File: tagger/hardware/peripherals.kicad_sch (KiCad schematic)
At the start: 15 parts, among them J2 MICRO_SD_CARD, U1 LSM6DS3, U8 MAX98357A, U9 W25Q128JVP

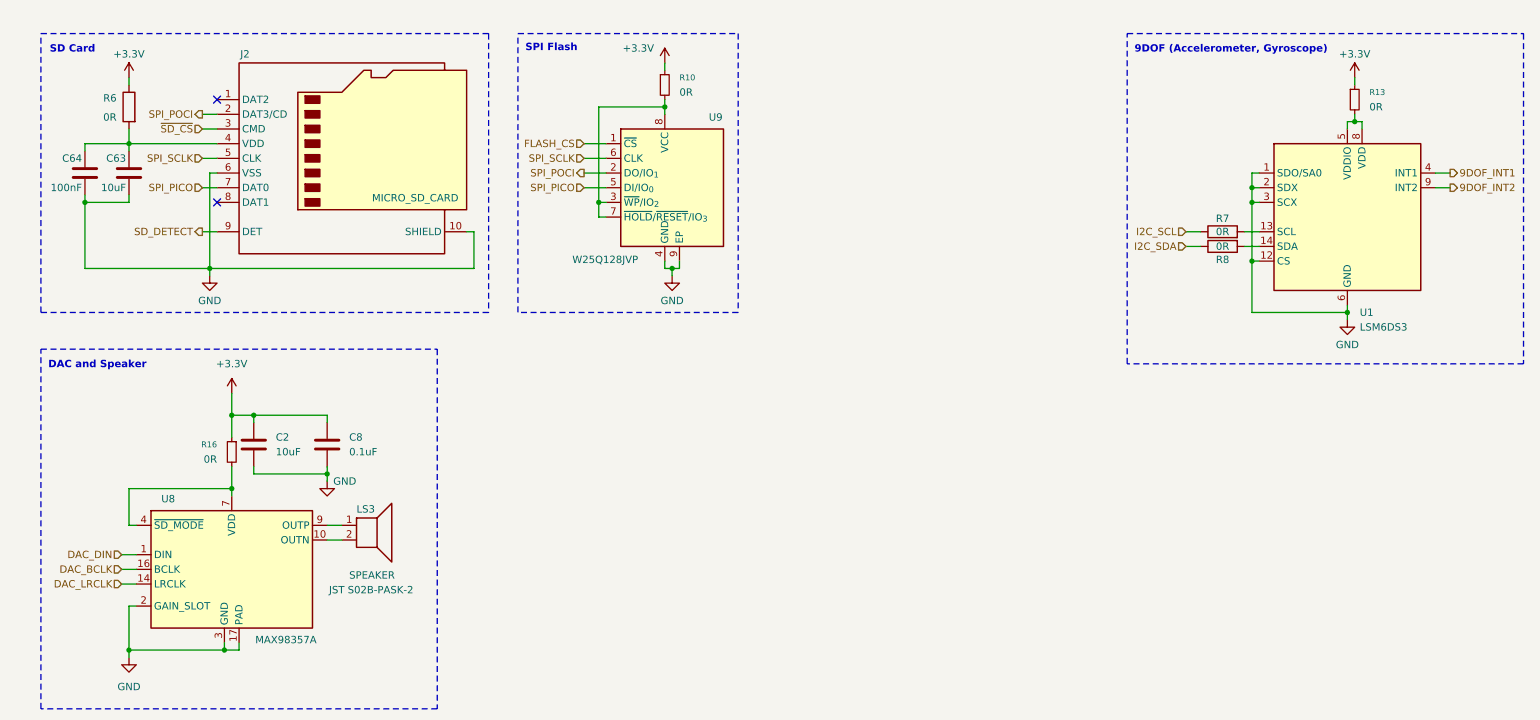
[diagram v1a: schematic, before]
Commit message: feat: various board routing changes
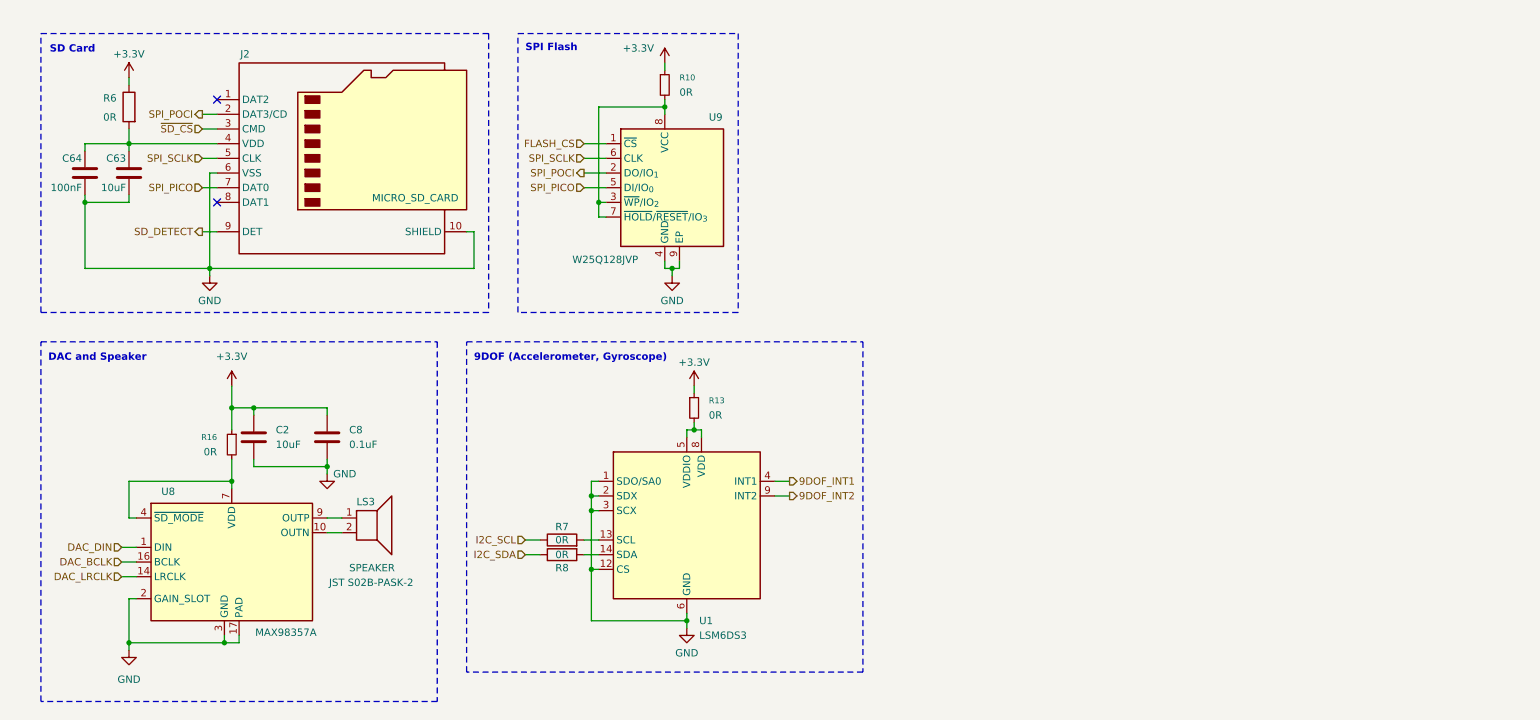
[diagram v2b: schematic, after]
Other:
- moved on the sheet: C2, C8, LS3, R13, R16, R7, R8, U1, U8

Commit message: feat: add IR routing, fix component sizes
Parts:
- C2, C63, C64, C8: footprint Capacitor_SMD:C_0201_0603Metric_Pad0.64x0.40mm_HandSolder -> Capacitor_SMD:C_0402_1005Metric
- R10, R13, R16, R6, R7, R8: footprint Resistor_SMD:R_0201_0603Metric_Pad0.64x0.40mm_HandSolder -> Resistor_SMD:R_0402_1005Metric
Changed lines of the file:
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@@
 			)
 		)
-		(property "Footprint" "Resistor_SMD:R_0201_0603Metric_Pad0.64x0.40mm_HandSolder"
+		(property "Footprint" "Resistor_SMD:R_0402_1005Metric"
 			(at 128.27 27.94 0)
 			(effects
@@
 			)
 		)
-		(property "Footprint" "Resistor_SMD:R_0201_0603Metric_Pad0.64x0.40mm_HandSolder"
+		(property "Footprint" "Resistor_SMD:R_0402_1005Metric"
 			(at 110.49 107.442 90)
 			(effects
@@
 			)
 		)
-		(property "Footprint" "Capacitor_SMD:C_0201_0603Metric_Pad0.64x0.40mm_HandSolder"
+		(property "Footprint" "Capacitor_SMD:C_0402_1005Metric"
 			(at 34.5948 46.99 0)
 			(effects
@@
 			)
 		)
-		(property "Footprint" "Capacitor_SMD:C_0201_0603Metric_Pad0.64x0.40mm_HandSolder"
+		(property "Footprint" "Capacitor_SMD:C_0402_1005Metric"
 			(at 58.1152 92.71 0)
 			(effects
@@
 			)
 		)
-		(property "Footprint" "Resistor_SMD:R_0201_0603Metric_Pad0.64x0.40mm_HandSolder"
+		(property "Footprint" "Resistor_SMD:R_0402_1005Metric"
 			(at 37.338 31.75 90)
 			(effects
@@
 			)
 		)
-		(property "Footprint" "Resistor_SMD:R_0201_0603Metric_Pad0.64x0.40mm_HandSolder"
+		(property "Footprint" "Resistor_SMD:R_0402_1005Metric"
 			(at 110.49 108.458 90)
 			(effects
@@
 			)
 		)
-		(property "Footprint" "Resistor_SMD:R_0201_0603Metric_Pad0.64x0.40mm_HandSolder"
+		(property "Footprint" "Resistor_SMD:R_0402_1005Metric"
 			(at 133.35 83.82 0)
 			(effects
@@
 			)
 		)
-		(property "Footprint" "Resistor_SMD:R_0201_0603Metric_Pad0.64x0.40mm_HandSolder"
+		(property "Footprint" "Resistor_SMD:R_0402_1005Metric"
 			(at 53.34 90.17 0)
 			(effects
@@
 			)
 		)
-		(property "Footprint" "Capacitor_SMD:C_0201_0603Metric_Pad0.64x0.40mm_HandSolder"
+		(property "Footprint" "Capacitor_SMD:C_0402_1005Metric"
 			(at 70.8152 92.71 0)
 			(effects
@@
 			)
 		)
-		(property "Footprint" "Capacitor_SMD:C_0201_0603Metric_Pad0.64x0.40mm_HandSolder"
+		(property "Footprint" "Capacitor_SMD:C_0402_1005Metric"
 			(at 26.9748 46.99 0)
 			(effects

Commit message: feat: added missing 3d models
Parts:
- LS3: footprint Connector_PinHeader_2.00mm:PinHeader_1x02_P2.00mm_Horizontal -> tagger:S02B-PASK-2
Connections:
- net SPI_PICO: now also U9.2 (DO/IO_{1}); no longer U9.5 (DI/IO_{0})
- net SPI_POCI: now also U9.5 (DI/IO_{0}); no longer U9.2 (DO/IO_{1})
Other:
- moved on the sheet: R10, R13, R7, R8, U1, U9

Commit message: feat: audio routing and test points
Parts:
- added JP2: GAIN, Jumper:SolderJumper-3_P1.3mm_Bridged12_RoundedPad1.0x1.5mm_NumberLabels, symbol Jumper:Jumper_3_Bridged12
- C2, C8: symbol Device:C -> Device:C_Small
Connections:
- net GND: now also JP2.3 (B)
- net at R16.2, U8.7 (VDD), U8.8 (VDD): now also JP2.1 (A); no longer U8.4 (~{SD_MODE})
- new net: JP2.2 (C), U8.4 (~{SD_MODE})
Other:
- note added: "NOTE: Could add a 5v regulator for DAC to increase speaker output power."
- moved on the sheet: C2, C8, LS3, R16, U8

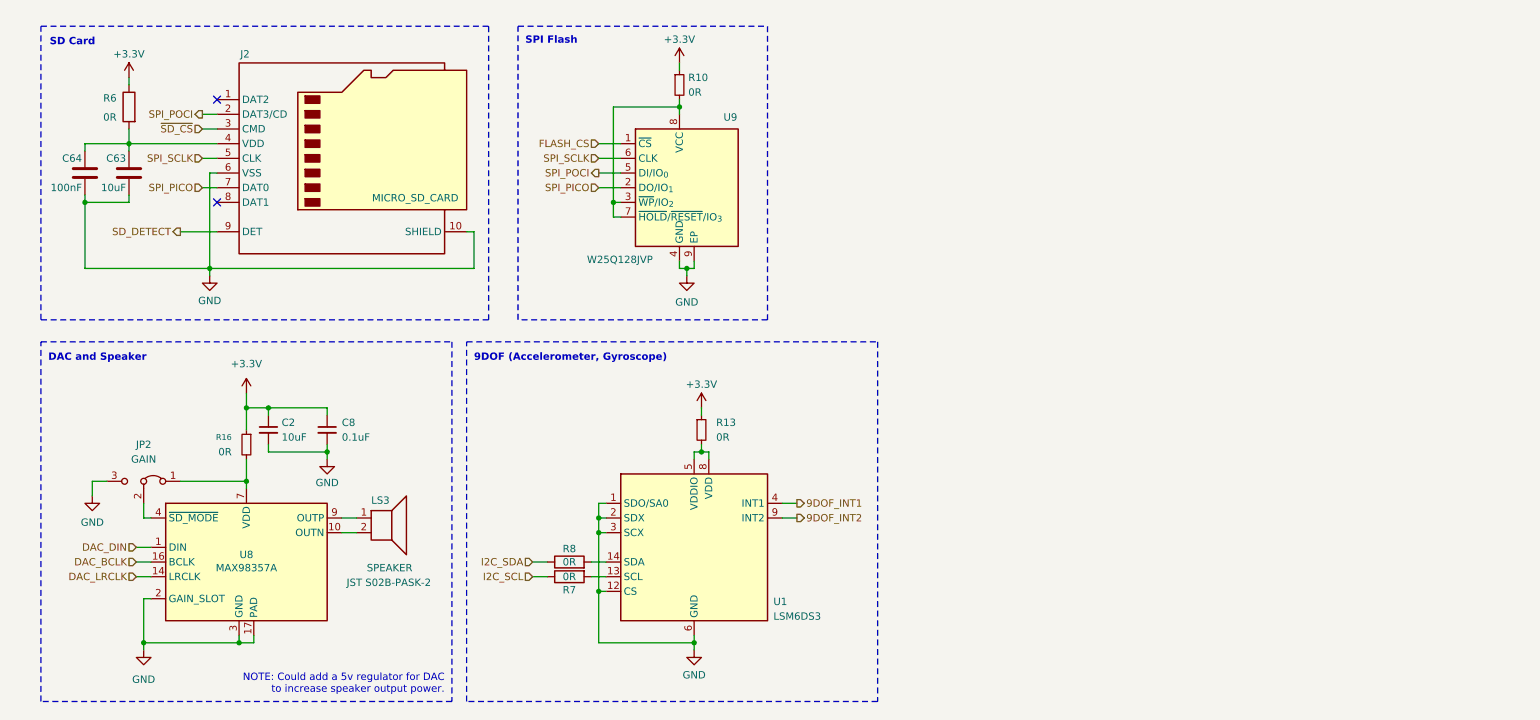
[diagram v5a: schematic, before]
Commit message: feat: schematic organization, added SD card connections
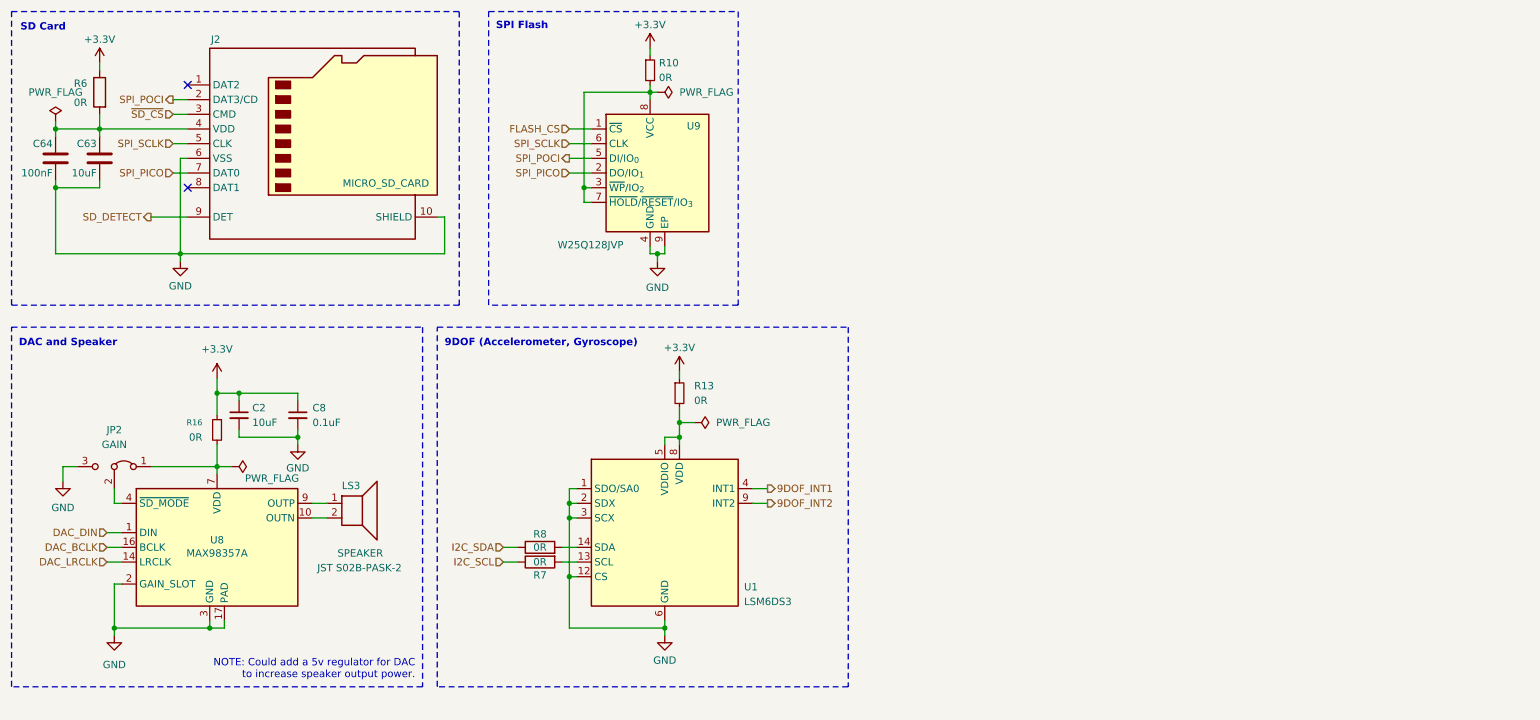
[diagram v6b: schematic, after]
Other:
- moved on the sheet: C2, C63, C64, C8, J2, JP2, LS3, R10, R13, R16, R6, R7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

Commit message: feat: replace RS485 transceiver, fix DRC warnings
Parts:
- LS3: now not fitted
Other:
- moved on the sheet: C2, C8, JP2, R10, R13, R16, R7, R8, U1, U8, U9
